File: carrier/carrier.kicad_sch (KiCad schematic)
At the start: 0 parts

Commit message: Feat: created CM4 schematic with modifications to fit needs
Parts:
- added H1, H2, H3, H4, H5, H6, H7, H8: MountingHole, MountingHole:MountingHole_2.7mm_M2.5, symbol Mechanical:MountingHole
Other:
- added sheet CM4_GPIO ( Ethernet, GPIO, SDCARD) (CM4_GPIO.kicad_sch)
- added sheet CM4_HighSpeed (CM4_HighSpeed.kicad_sch)
- added sheet USB2-HUB (USB2-HUB.kicad_sch)
- note added: "Clean (reverse polarity protected) 5V is expected"
- note added: "Connectors ------- Dual USB microUSB"
- note added: "Connectors ------- Ethernet 40way RPI Jumpers"
- note added: "Connectors ------- HDMI 0 HDMI 1 CSI 0 CSI 1 DSI 0 DSI 1"
- company: (none) -> MUREX
- title: (none) -> Carrier Board

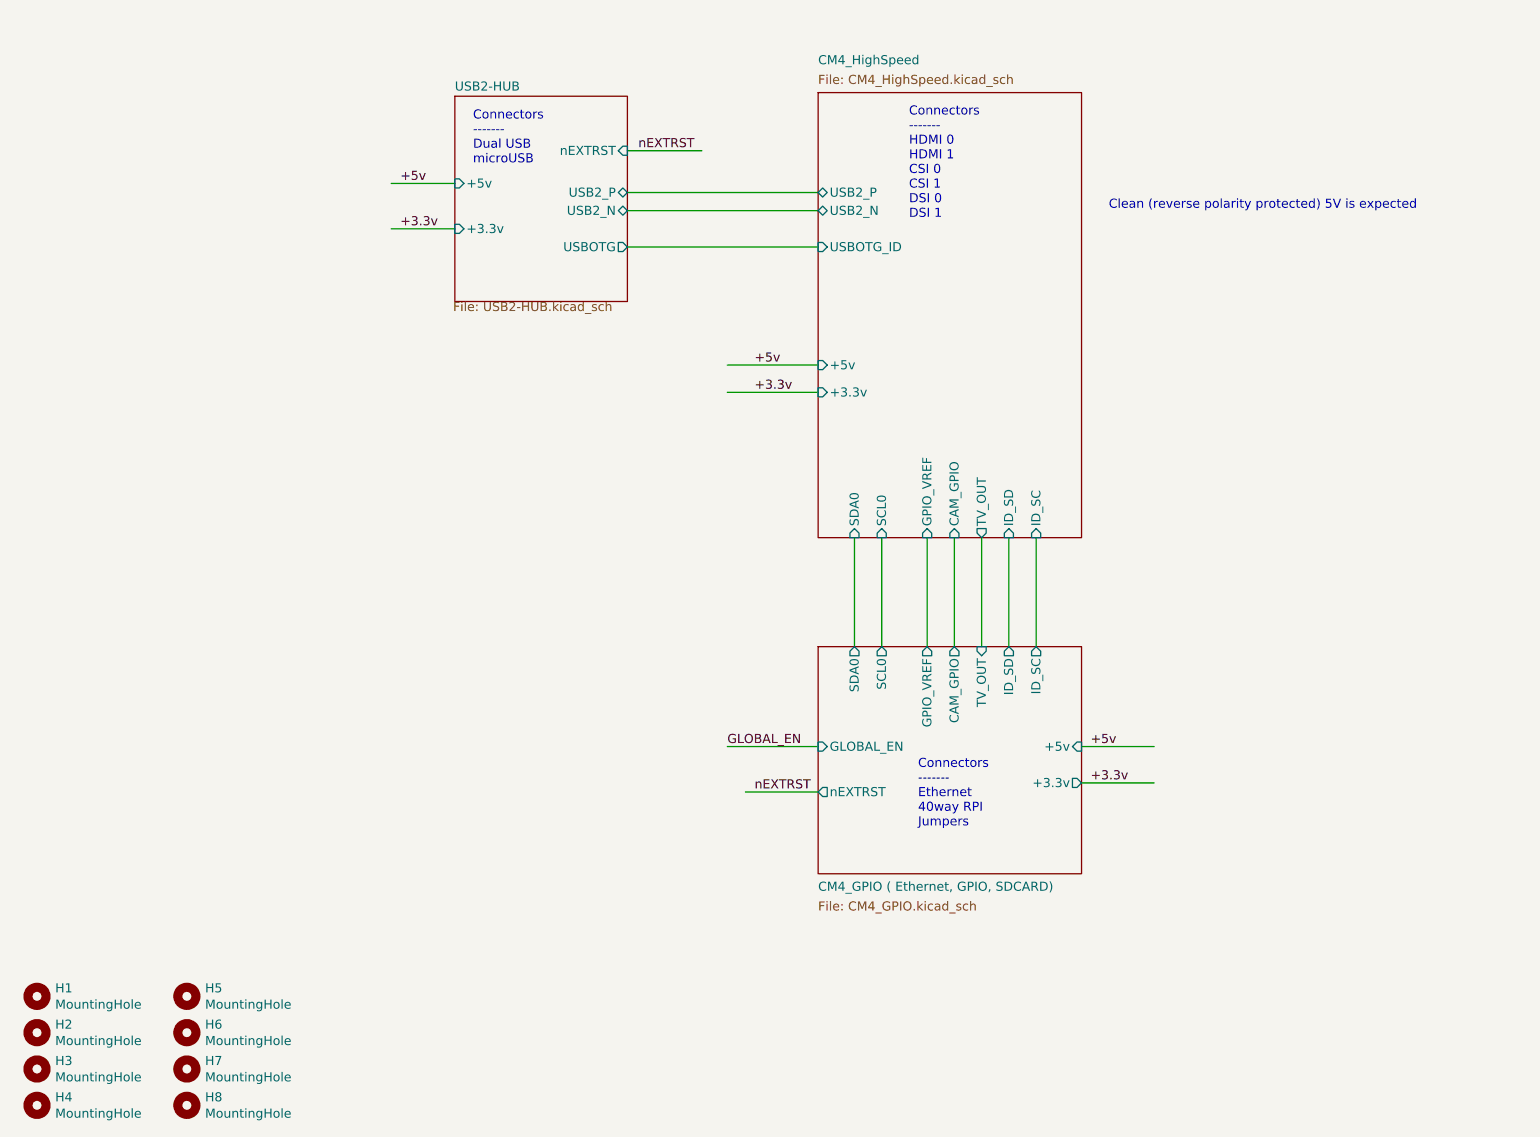
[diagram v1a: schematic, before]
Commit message: Feat: added all sensors, neopixel, buzzer and usb-c to carrier board
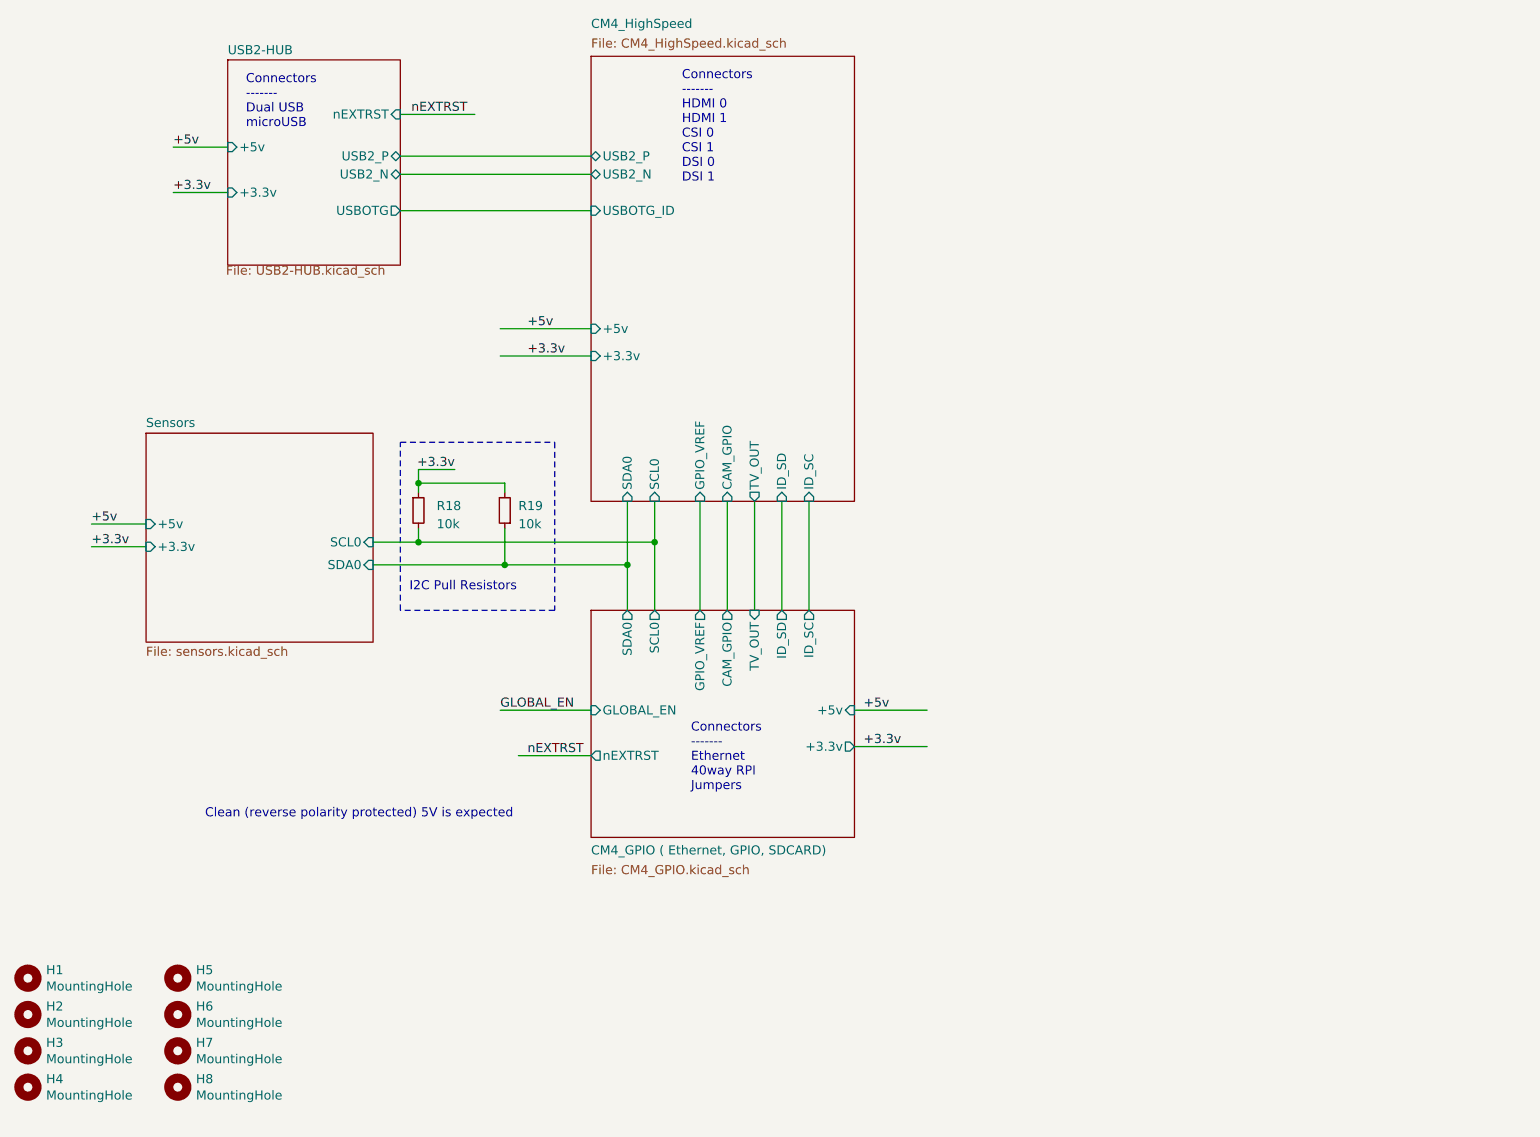
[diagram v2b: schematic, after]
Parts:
- added R18, R19: 10k, symbol Device:R_Small
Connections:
- net +3.3v: now also R18.1, R19.2
- net CM4_GPIO ( Ethernet, GPIO, SDCARD)/SCL0: now also R18.2
- net CM4_GPIO ( Ethernet, GPIO, SDCARD)/SDA0: now also R19.1
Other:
- added sheet Sensors (sensors.kicad_sch)
- note added: "I2C Pull Resistors"
- moved on the sheet: H1, H2, H3, H4, H5, H6, H7, H8

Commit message: Feat: carrier board synchronized footprints with schematic
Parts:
- R18, R19: footprint (none) -> Resistor_SMD:R_0603_1608Metric
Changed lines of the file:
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@@
       (effects (font (size 1.27 1.27)) (justify left))
     )
-    (property "Footprint" "" (at 77.47 101.6 0)
+    (property "Footprint" "Resistor_SMD:R_0603_1608Metric" (at 77.47 101.6 0)
       (effects (font (size 1.27 1.27)) hide)
     )
@@
       (effects (font (size 1.27 1.27)) (justify right))
     )
-    (property "Footprint" "" (at 89.535 101.6 0)
+    (property "Footprint" "Resistor_SMD:R_0603_1608Metric" (at 89.535 101.6 0)
       (effects (font (size 1.27 1.27)) hide)
     )

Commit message: Fix: fixed 3D models for carrier board
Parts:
- renumbered R18 to R1, R19 to R2
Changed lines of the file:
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@@
   (symbol (lib_id "Device:R_Small") (at 77.47 101.6 0) (unit 1)
     (in_bom yes) (on_board yes) (dnp no) (fields_autoplaced)
-    (property "Reference" "R18" (at 80.01 100.965 0)
+    (property "Reference" "R1" (at 80.01 100.965 0)
       (effects (font (size 1.27 1.27)) (justify left))
     )
@@
       (project "carrier"
         (path "/4b1cea9d-93bc-4380-88c3-ede99bb53de2"
-          (reference "R18") (unit 1)
+          (reference "R1") (unit 1)
         )
       )
@@
   (symbol (lib_id "Device:R_Small") (at 89.535 101.6 180) (unit 1)
     (in_bom yes) (on_board yes) (dnp no) (fields_autoplaced)
-    (property "Reference" "R19" (at 91.44 100.965 0)
+    (property "Reference" "R2" (at 91.44 100.965 0)
       (effects (font (size 1.27 1.27)) (justify right))
     )
@@
       (project "carrier"
         (path "/4b1cea9d-93bc-4380-88c3-ede99bb53de2"
-          (reference "R19") (unit 1)
-        )
-      )
+          (reference "R2") (unit 1)
+        )
+      )

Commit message: Refactor: cleaned up libraries
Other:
- added sheet Connectors (connectors.kicad_sch)
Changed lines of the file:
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@@
   )
   (sheet (at 101.6 38.1) (size 36.83 62.23)
-    (stroke (width 0.1524) (type solid) (color 132 0 132 1))
-    (fill (color 255 255 255 0.0000))
+    (stroke (width 0.1524) (type solid))
+    (fill (color 0 0 0 0.0000))
     (property "Sheetname" "CM4_HighSpeed" (at 101.6 34.29 0)
       (effects (font (size 1.27 1.27)) (justify left bottom))
@@
   )
   (sheet (at 101.6 115.57) (size 36.83 31.75)
-    (stroke (width 0.1524) (type solid) (color 132 0 132 1))
-    (fill (color 255 255 255 0.0000))
+    (stroke (width 0.1524) (type solid))
+    (fill (color 0 0 0 0.0000))
     (property "Sheetname" "CM4_GPIO ( Ethernet, GPIO, SDCARD)" (at 101.6 149.86 0)
       (effects (font (size 1.27 1.27)) (justify left bottom))
@@
     )
   )
+  (sheet (at 151.765 115.57) (size 34.29 31.75) (fields_autoplaced)
+    (stroke (width 0.1524) (type solid))
+    (fill (color 0 0 0 0.0000))
+    (property "Sheetname" "Connectors" (at 151.765 114.8584 0)
+      (effects (font (size 1.27 1.27)) (justify left bottom))
+    )
+    (property "Sheetfile" "connectors.kicad_sch" (at 151.765 147.9046 0)
+      (effects (font (size 1.27 1.27)) (justify left top))
+    )
+    (instances
+      (project "carrier"
+        (path "/4b1cea9d-93bc-4380-88c3-ede99bb53de2" (page "7"))
+      )
+    )
+  )
   (sheet (at 50.8 38.608) (size 24.13 28.702)
-    (stroke (width 0.1524) (type solid) (color 132 0 132 1))
-    (fill (color 255 255 255 0.0000))
+    (stroke (width 0.1524) (type solid))
+    (fill (color 0 0 0 0.0000))
     (property "Sheetname" "USB2-HUB" (at 50.8 37.9725 0)
       (effects (font (size 1.27 1.27)) (justify left bottom))

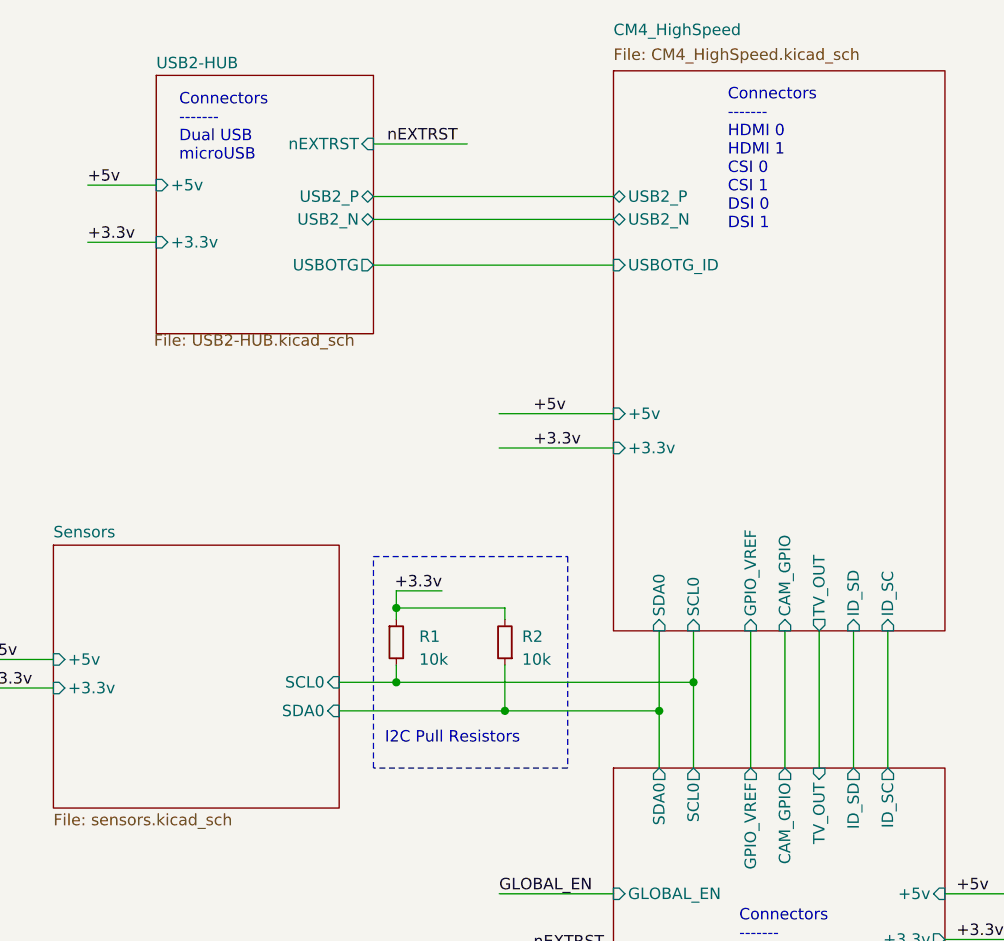
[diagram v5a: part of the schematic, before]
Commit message: Refactor: small changes for carrier, cm4 and leaksensors
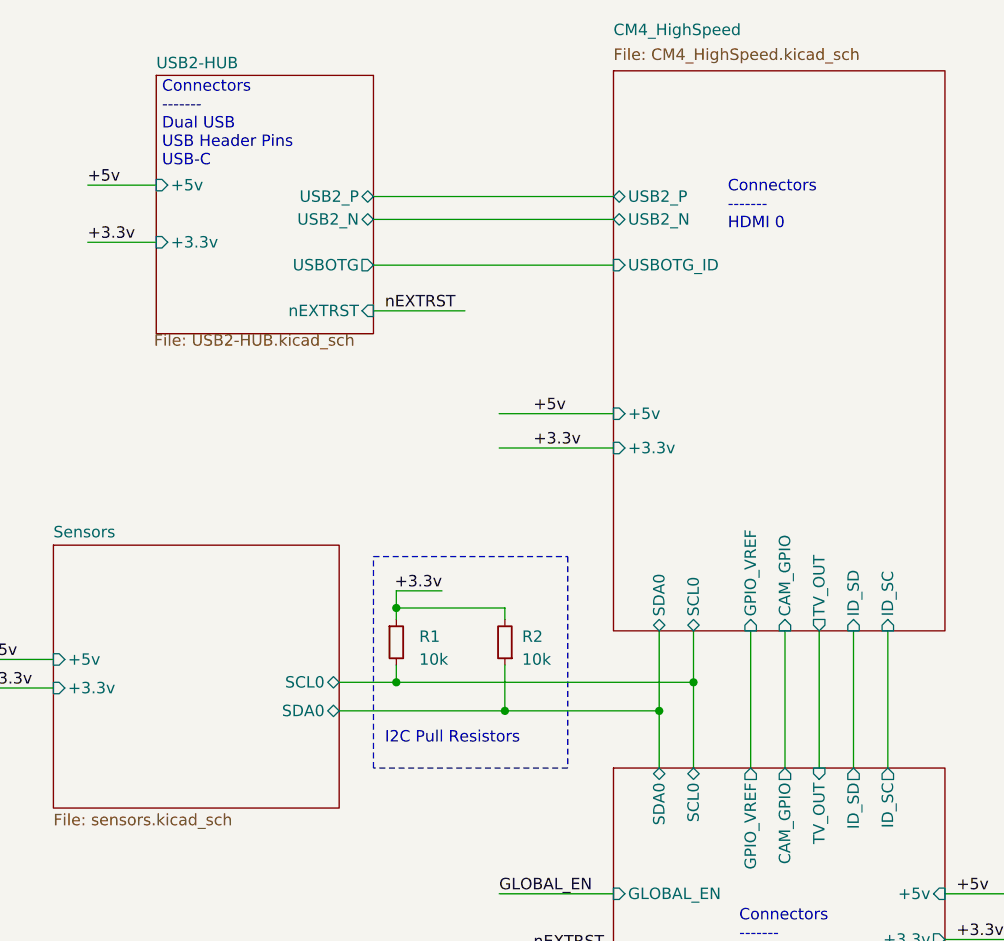
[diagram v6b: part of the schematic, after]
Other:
- note added: "Connectors ------- Dual USB USB Header Pins USB-C"
- note added: "Connectors ------- HDMI 0"
- note removed: "Connectors ------- Dual USB microUSB"
- note removed: "Connectors ------- HDMI 0 HDMI 1 CSI 0 CSI 1 DSI 0 DSI 1"
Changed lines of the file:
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@@
     (stroke (width 0) (type default))
+  )
+  (wire (pts (xy 74.93 64.77) (xy 85.09 64.77))
+    (stroke (width 0) (type solid))
   )
   (wire (pts (xy 116.84 100.33) (xy 116.84 115.57))
@@
   )
   (wire (pts (xy 106.68 109.22) (xy 106.68 115.57))
-    (stroke (width 0) (type solid))
-  )
-  (wire (pts (xy 74.93 46.228) (xy 85.344 46.228))
     (stroke (width 0) (type solid))
   )
@@
     (effects (font (size 1.27 1.27)) (justify left bottom))
   )
-  (text "Connectors\n-------\nDual USB\nmicroUSB" (exclude_from_sim no)
- (at 53.34 48.26 0)
-    (effects (font (size 1.27 1.27)) (justify left bottom))
-  )
-  (text "Connectors\n-------\nHDMI 0\nHDMI 1\nCSI 0\nCSI 1\nDSI 0\nDSI 1" (exclude_from_sim no)
-    (at 114.3 55.88 0)
+  (text "Connectors\n-------\nDual USB\nUSB Header Pins\nUSB-C" (exclude_from_sim no)
+ (at 51.435 48.895 0)
+    (effects (font (size 1.27 1.27)) (justify left bottom))
+  )
+  (text "Connectors\n-------\nHDMI 0" (exclude_from_sim no)
+ (at 114.3 55.88 0)
     (effects (font (size 1.27 1.27)) (justify left bottom))
   )
@@
     (effects (font (size 1.27 1.27)) (justify left bottom))
   )
-  (label "nEXTRST" (at 76.454 46.228 0) (fields_autoplaced)
+  (label "nEXTRST" (at 76.2 64.77 0) (fields_autoplaced)
     (effects (font (size 1.27 1.27)) (justify left bottom))
   )
@@
       (effects (font (size 1.27 1.27)) (justify left))
     )
-    (pin "SCL0" input (at 110.49 100.33 270)
-      (effects (font (size 1.27 1.27)) (justify left))
-    )
-    (pin "SDA0" input (at 106.68 100.33 270)
+    (pin "SCL0" bidirectional (at 110.49 100.33 270)
+      (effects (font (size 1.27 1.27)) (justify left))
+    )
+    (pin "SDA0" bidirectional (at 106.68 100.33 270)
       (effects (font (size 1.27 1.27)) (justify left))
     )
@@
       (effects (font (size 1.27 1.27)) (justify right))
     )
-    (pin "SCL0" output (at 110.49 115.57 90)
-      (effects (font (size 1.27 1.27)) (justify right))
-    )
-    (pin "SDA0" output (at 106.68 115.57 90)
+    (pin "SCL0" bidirectional (at 110.49 115.57 90)
+      (effects (font (size 1.27 1.27)) (justify right))
+    )
+    (pin "SDA0" bidirectional (at 106.68 115.57 90)
       (effects (font (size 1.27 1.27)) (justify right))
     )
@@
       (effects (font (size 1.27 1.27)) hide)
     )
-    (pin "SDA0" input (at 71.12 109.22 0)
-      (effects (font (size 1.27 1.27)) (justify right))
-    )
-    (pin "SCL0" input (at 71.12 106.045 0)
+    (pin "SDA0" bidirectional (at 71.12 109.22 0)
+      (effects (font (size 1.27 1.27)) (justify right))
+    )
+    (pin "SCL0" bidirectional (at 71.12 106.045 0)
       (effects (font (size 1.27 1.27)) (justify right))
     )
@@
       (effects (font (size 1.27 1.27)) (justify left))
     )
-    (pin "nEXTRST" input (at 74.93 46.228 0)
-      (effects (font (size 1.27 1.27)) (justify right))
-    )
+    (pin "nEXTRST" input (at 74.93 64.77 0)
+      (effects (font (size 1.27 1.27)) (justify right))
+    )
